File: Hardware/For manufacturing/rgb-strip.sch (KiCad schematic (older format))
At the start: 14 parts, among them CON1 BARREL_JACK, IC1 ATTINY84-P, K1 CONN_3_V, P1 BT_Header-1x06, P2 CONN_01X02, Q1 HC49, SW1 SW_PUSH, U1 7805, U2 ICSP

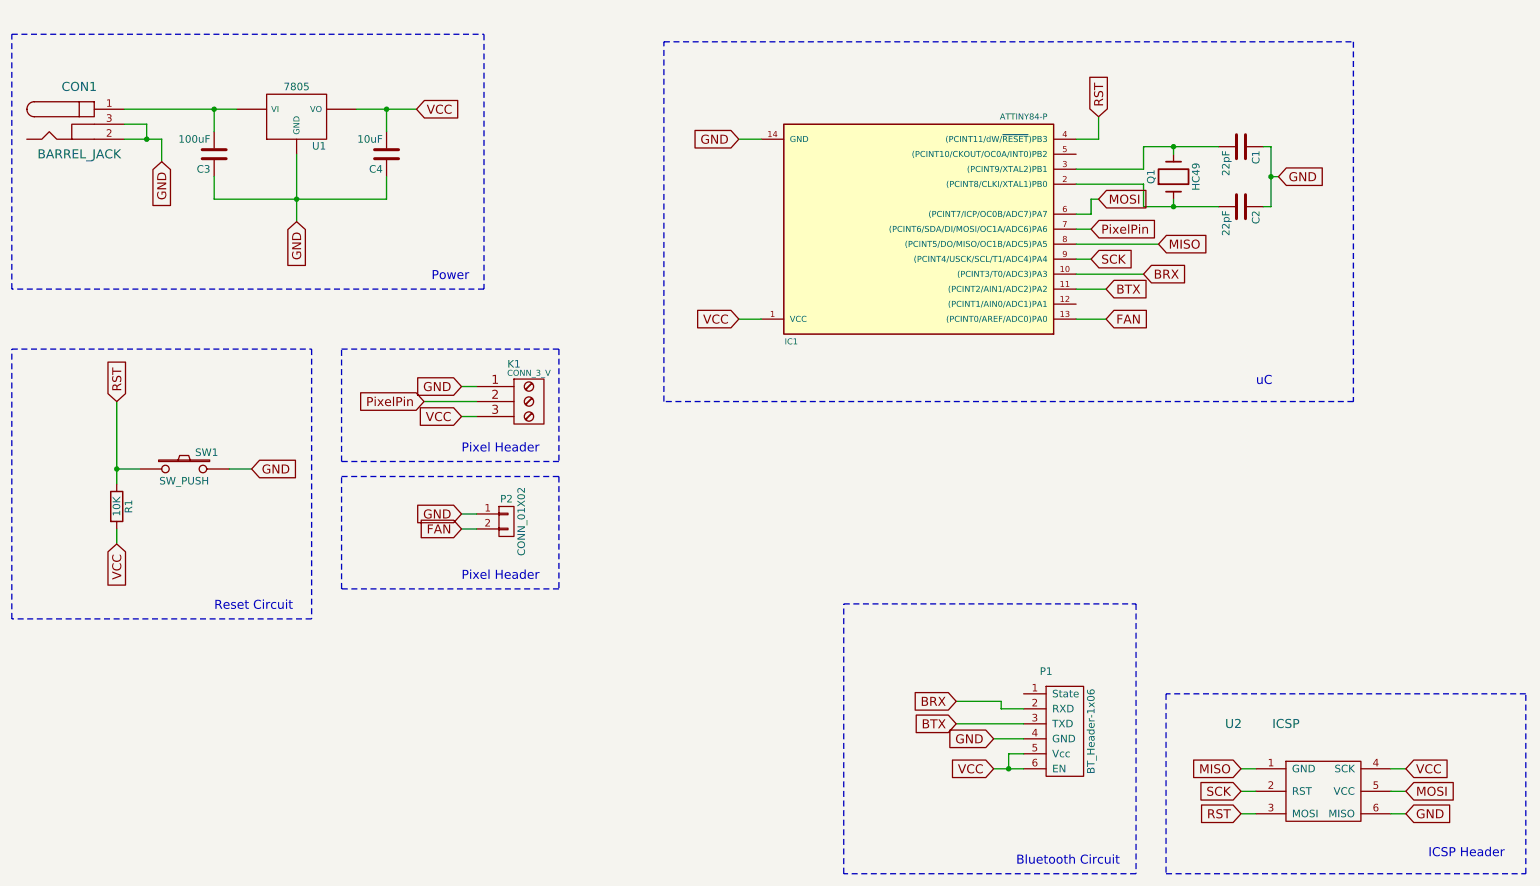
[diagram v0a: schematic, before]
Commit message: Finished board - minor improvements - Removed fan support
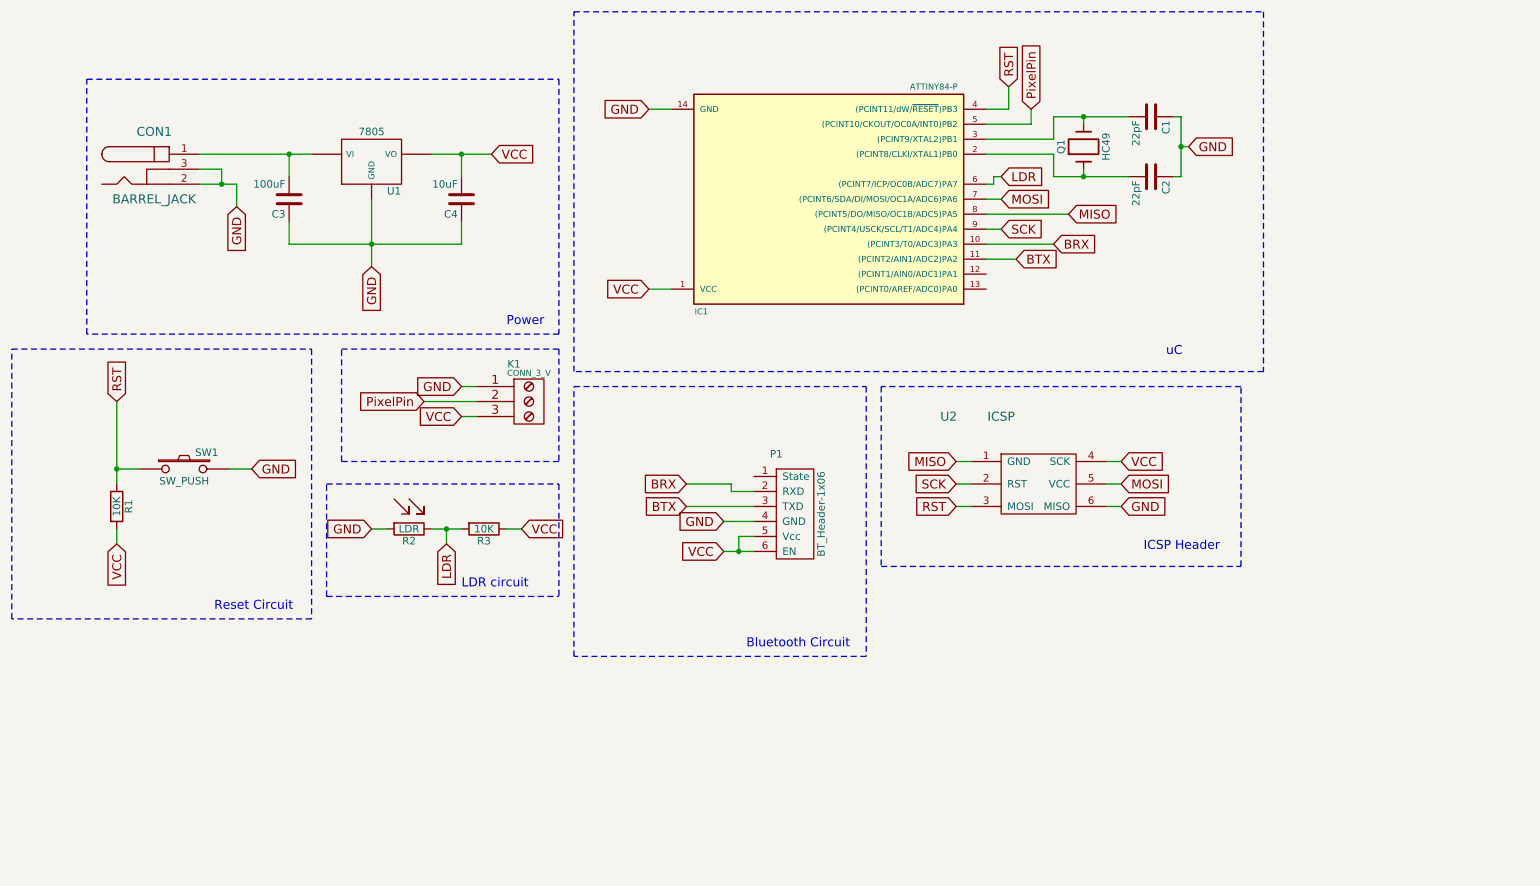
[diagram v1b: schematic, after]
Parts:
- removed P2: CONN_01X02, Pin_Headers:Pin_Header_Straight_1x02, symbol CONN_01X02
- added R2: LDR, symbol LDR
- added R3: 10K, Resistors_ThroughHole:Resistor_Horizontal_RM10mm, symbol R
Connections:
- net GND: now also R2.2
- net MOSI: now also IC1.7 ((PCINT6/SDA/DI/MOSI/OC1A/ADC6)PA6); no longer IC1.6 ((PCINT7/ICP/OC0B/ADC7)PA7)
- net PixelPin: now also IC1.5 ((PCINT10/CKOUT/OC0A/INT0)PB2); no longer IC1.7 ((PCINT6/SDA/DI/MOSI/OC1A/ADC6)PA6)
- net VCC: now also R3.1
- net FAN: no longer names the net of IC1.13 ((PCINT0/AREF/ADC0)PA0)
- new net LDR: IC1.6 ((PCINT7/ICP/OC0B/ADC7)PA7), R2.1, R3.2
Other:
- note added: "LDR circuit"
- note removed: "Pixel Header"
- moved on the sheet: C1, C2, C3, C4, CON1, IC1, P1, Q1, U1, U2

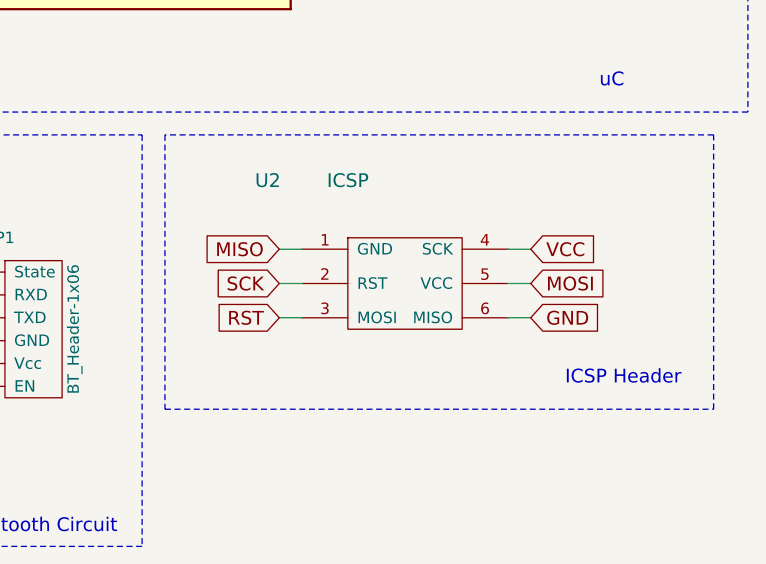
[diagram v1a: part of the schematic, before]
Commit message: Improved design and updated gerbers
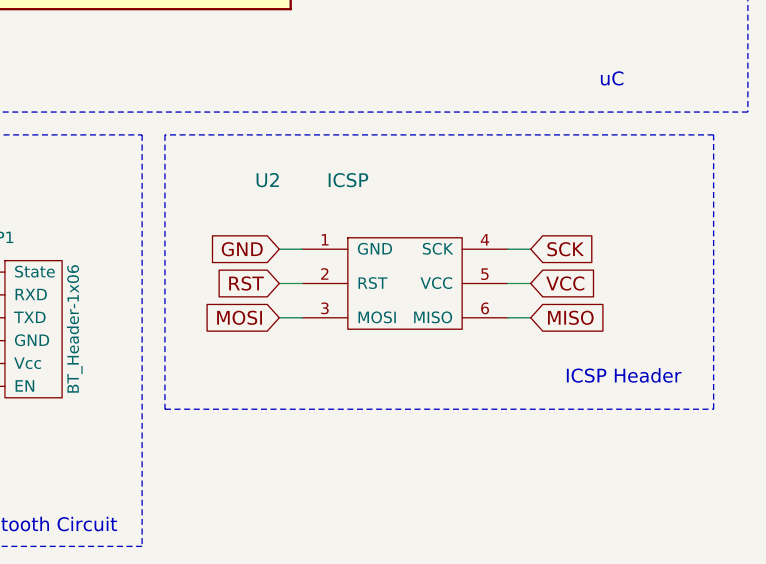
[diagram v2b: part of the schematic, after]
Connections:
- net GND: now also U2.1 (GND); no longer U2.6 (MISO)
- net MISO: now also U2.6 (MISO); no longer U2.1 (GND)
- net MOSI: now also U2.3 (MOSI); no longer U2.5 (VCC)
- net RST: now also U2.2 (RST); no longer U2.3 (MOSI)
- net SCK: now also U2.4 (SCK); no longer U2.2 (RST)
- net VCC: now also U2.5 (VCC); no longer U2.4 (SCK)
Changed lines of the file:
@@
 	1    0    0    -1
 $EndComp
+Text GLabel 7100 3700 0    60   Input ~ 0
+RST
+Text GLabel 7100 3550 0    60   Input ~ 0
+GND
+Text GLabel 8200 3700 2    60   Input ~ 0
+VCC
+Text GLabel 8200 3550 2    60   Input ~ 0
+SCK
+Text GLabel 8200 3850 2    60   Input ~ 0
+MISO
 Text GLabel 7100 3850 0    60   Input ~ 0
-RST
-Text GLabel 8200 3850 2    60   Input ~ 0
-GND
-Text GLabel 8200 3550 2    60   Input ~ 0
-VCC
-Text GLabel 7100 3700 0    60   Input ~ 0
-SCK
-Text GLabel 7100 3550 0    60   Input ~ 0
-MISO
-Text GLabel 8200 3700 2    60   Input ~ 0
 MOSI
 Text GLabel 7400 2000 2    60   Input ~ 0
